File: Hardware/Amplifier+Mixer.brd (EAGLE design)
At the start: 140 x 140 mm, 194 parts, among them IC1 7812, IC2 7805, IC3 7912, IC4 OPA134PA, IC5 OPA134PA, IC6 MEGA8-AI, IC8 LM358D, IC9 LM358D, J1 6MM, J10 JST-XH2, J2 6MM, J3 6MM, J4 6MM, J5 TERMINAL-BLOCK-2PLUG-IN, J6 TERMINAL-BLOCK-2PLUG-IN, J7 ENCODER, J8 DISPLAY, J9 USB, K1 12V 8A, K2 12V 8A, T1 BC817, T2 BC817, T3 BC817, U1 LM1117-3.3, U2 10k, U3 10k, U4 10k, U5 10k, U6 TDA7498L, U7 10k, U8 10k, U9 MCP9700SMD, X1 RCA-4-CHANNEL, X2 JST-XH2, X3 ICSP, X4 JST-XH2

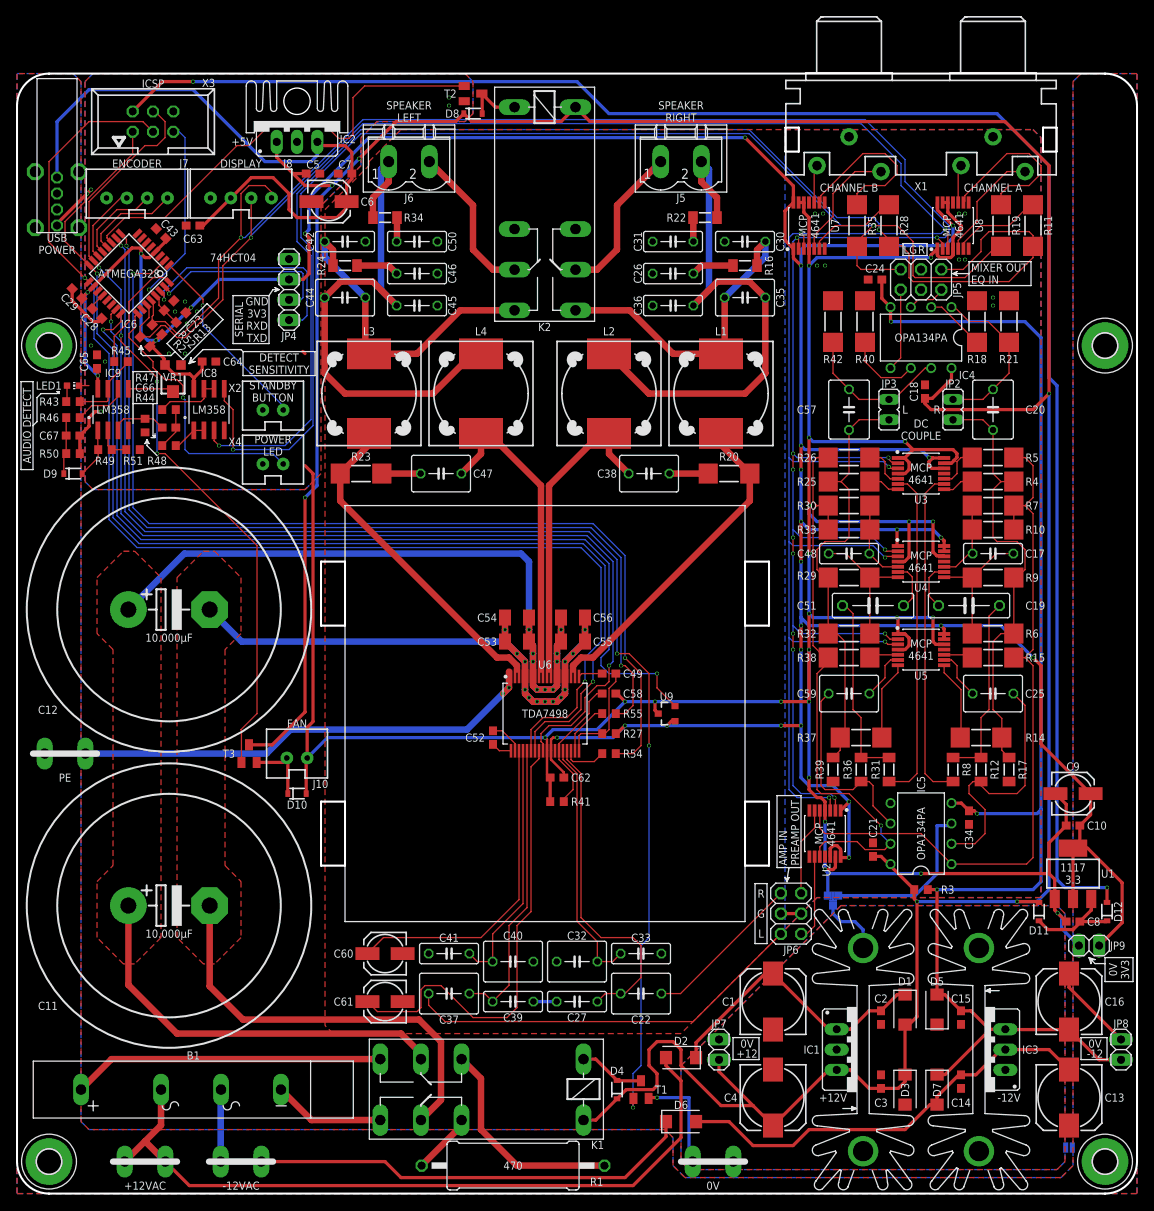
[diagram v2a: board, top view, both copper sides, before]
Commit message: moved power led to pwm capable pin
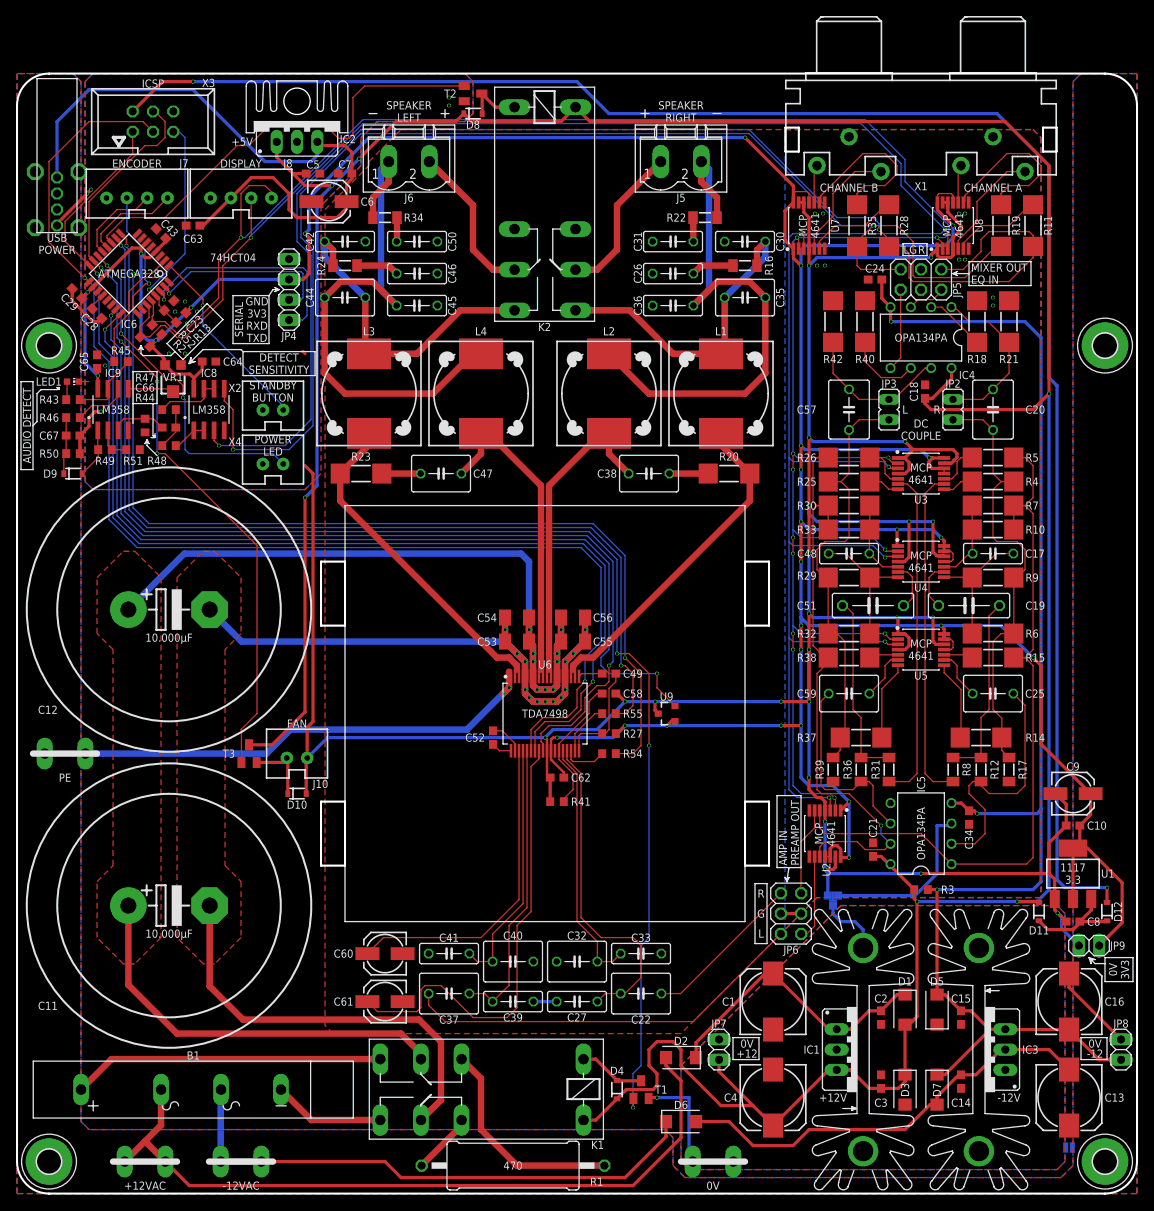
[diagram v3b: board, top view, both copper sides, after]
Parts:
- moved LED1 0.50 mm to (7.00, 101.5)
- moved R43 0.25 mm to (7.00, 99.2)
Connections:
- removed net N$45: IC6.14, J7.2
- new net ENC_BTN: IC6.25, J7.2
- net POWER_LED: now also IC6.14; no longer IC6.25
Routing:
- net ENC_BTN: track 0.00 -> 16.9 mm, vias 0 -> 1
- net +3V3: track 446.6 -> 461.5 mm
- net N$45: track 9.73 -> 0.00 mm
- net POWER_LED: track 34.2 -> 42.4 mm, vias 1 -> 3
- net T_SENSE: track 117.2 -> 116.2 mm
- net AUDIO_DETECT: track 14.8 -> 15.5 mm
- net DGND: vias 35 -> 34

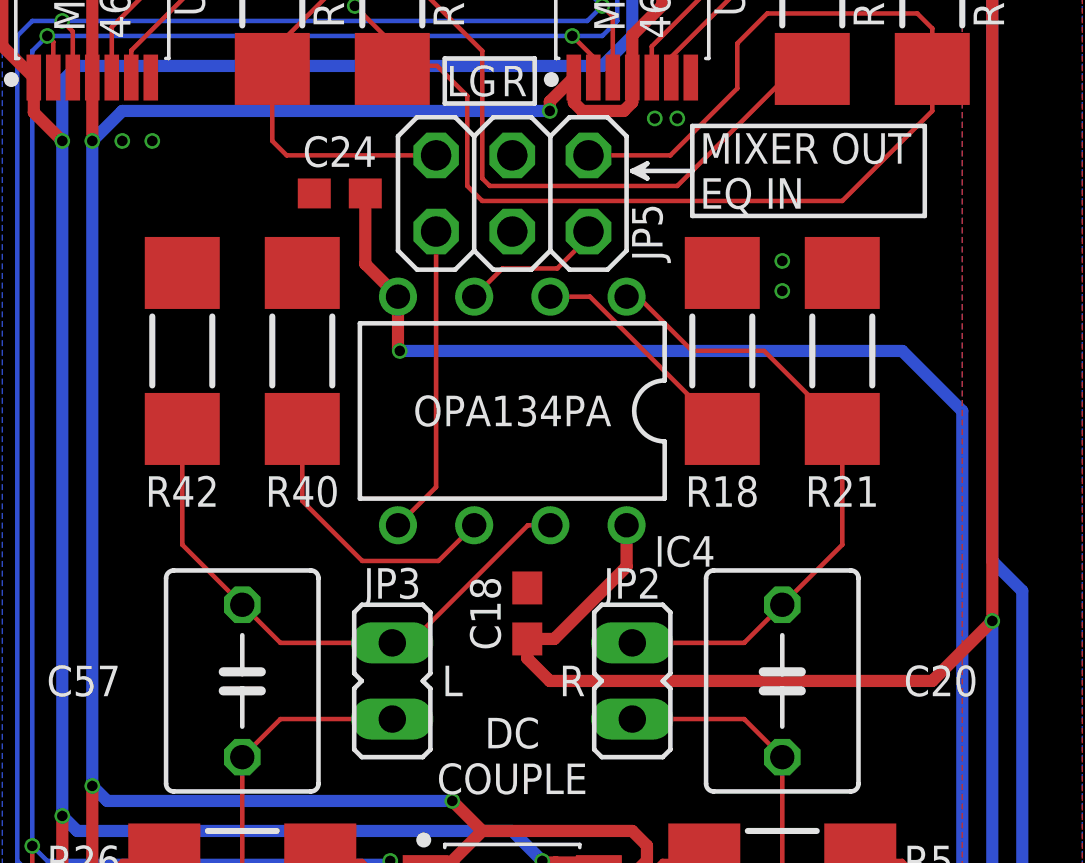
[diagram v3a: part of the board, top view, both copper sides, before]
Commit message: fixed feedback network in mixer buffer output stage
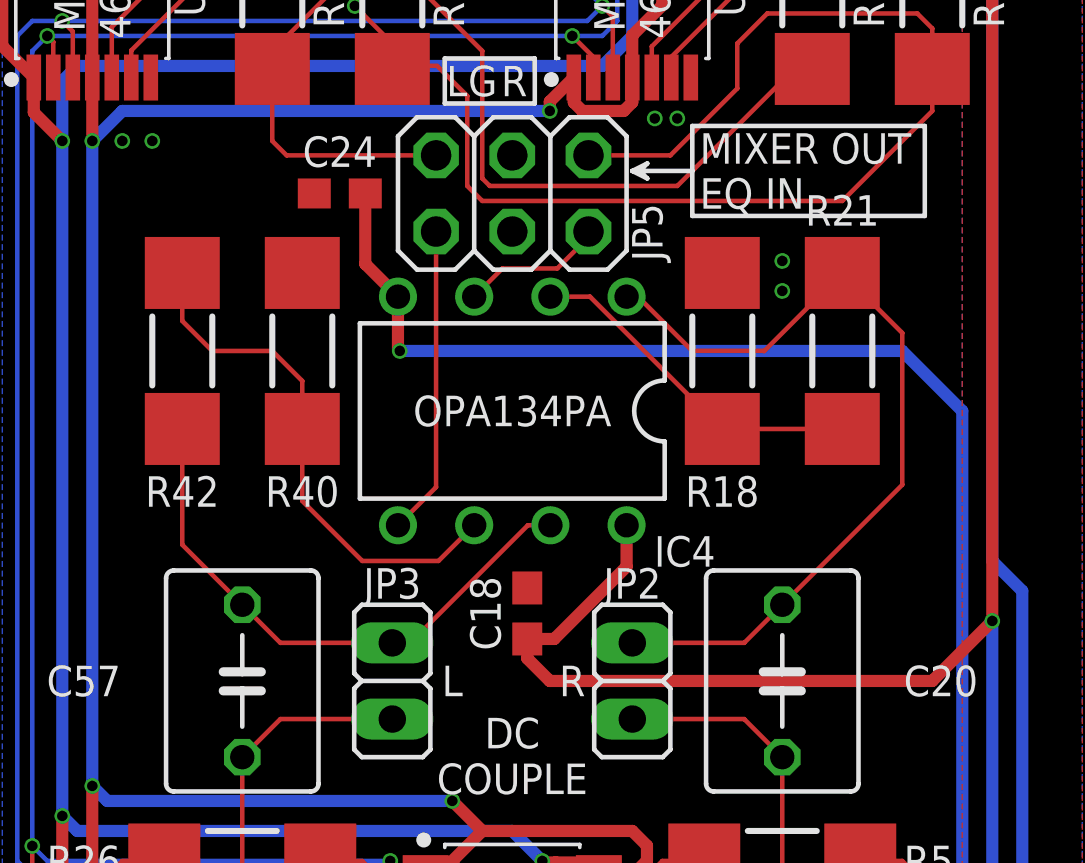
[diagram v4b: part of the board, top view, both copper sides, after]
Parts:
- added U$1: (no value), AdapterBoard:LOGO-SILKSCREEN
- IC4, IC5: value OPA134PA -> LME49720NA
- U9: value MCP9700SMD -> MCP9701SMD
- turned R21 to 270 degrees
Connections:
- removed net N$52: IC4.2, R18.1
- new net N$45: IC4.2, R18.1, R21.2
- net AGND: no longer R21.2, R42.2
- net N$44: now also R42.2
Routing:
- net N$45: track 0.00 -> 11.6 mm
- net N$44: track 9.45 -> 17.5 mm
- net N$52: track 7.56 -> 0.00 mm
- net MIX_AMP_R: track 21.2 -> 28.1 mm
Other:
- board text added: "+3V3"
- board text added: "AVR ICSP"
- board text added: "Amp In"
- board text added: "BTN"
- board text added: "Class D Amplifier 100W + 100 W"
- board text added: "Couple"
- board text added: "DC"
- board text added: "DC+"
- board text added: "DC-"
- board text added: "E A"
- board text added: "E B"
- board text added: "EQ In"
- board text added: "GND"
- board text added: "Mixer Out"
- board text added: "Preamp Out"
- board text added: "RXD"
- board text added: "SCL"
- board text added: "SDA"
- board text added: "Speaker Left"
- board text added: "Speaker Right"
- board text added: "TXD"
- board text added: "V+"
- board text added: "V-"
- board text added: "nupo-artworks.de"
- board text added: "~V+"
- board text added: "~V-"

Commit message: updated to newest version
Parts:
- IC1: value 7812 -> LM2940CT-12
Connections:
- new net VDD: C62.2, R27.2, U6.26
- net +3V3: no longer C62.2, R27.2, U6.26
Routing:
- net +3V3: track 461.5 -> 437.3 mm, vias 27 -> 25
- net VDD: track 0.00 -> 16.1 mm, vias 0 -> 2
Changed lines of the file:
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@@
 <setting verticaltext="up"/>
 </settings>
-<grid distance="1" unitdist="mm" unit="mm" style="lines" multiple="1" display="yes" altdistance="0.25" altunitdist="mm" altunit="mm"/>
+<grid distance="1" unitdist="mm" unit="mm" style="lines" multiple="1" display="yes" altdistance="0.5" altunitdist="mm" altunit="mm"/>
 <layers>
 <layer number="1" name="Top" color="4" fill="1" visible="yes" active="yes"/>
@@
 <attribute name="STOCK" value="4" x="4" y="4" size="1.778" layer="27" display="off"/>
 </element>
-<element name="IC1" library="v-reg" library_urn="urn:adsk.eagle:library:409" package="78XXS" package3d_urn="urn:adsk.eagle:package:30342/1" value="7812" x="105" y="18" smashed="yes" rot="R270">
-<attribute name="CONRAD" value="179230 - 62" x="105" y="18" size="1.778" layer="27" rot="R270" display="off"/>
+<element name="IC1" library="v-reg" library_urn="urn:adsk.eagle:library:409" package="78XXS" package3d_urn="urn:adsk.eagle:package:30342/1" value="LM2940CT-12" x="105" y="18" smashed="yes" rot="R270">
+<attribute name="CONRAD" value="1013996 - 62" x="105" y="18" size="1.778" layer="27" rot="R270" display="off"/>
 <attribute name="MOUSER" value="511-L7812CV" x="105" y="18" size="1.778" layer="27" rot="R270" display="off"/>
 <attribute name="NAME" x="100.3558" y="18" size="1.016" layer="25" ratio="14" align="center-right"/>
@@
 <contactref element="C9" pad="+"/>
 <contactref element="C10" pad="1"/>
-<contactref element="R27" pad="2"/>
-<contactref element="C62" pad="2"/>
 <contactref element="U7" pad="1"/>
 <contactref element="U8" pad="14"/>
@@
 <contactref element="R2" pad="2"/>
 <contactref element="R52" pad="2"/>
-<contactref element="U6" pad="26"/>
 <wire x1="10.095" y1="100.6" x2="10.095" y2="102.25" width="0.4064" layer="1"/>
 <wire x1="16.601040625" y1="105.89895625" x2="17.35104375" y2="106.648959375" width="0.4064" layer="1"/>
@@
 <wire x1="102.95" y1="42.1134" x2="102.95" y2="43.05" width="0.4064" layer="1"/>
 <wire x1="102.95" y1="43.05" x2="102.5" y2="43.5" width="0.4064" layer="1"/>
-<wire x1="74.85" y1="57.5" x2="75" y2="57.5" width="0.4064" layer="1"/>
-<wire x1="75" y1="57.5" x2="76" y2="58.5" width="0.4064" layer="1"/>
-<via x="76" y="58.5" extent="1-16" drill="0.35" shape="octagon"/>
-<wire x1="95.5" y1="58.5" x2="81.25" y2="58.5" width="0.4064" layer="16"/>
+<wire x1="95.5" y1="58.5" x2="83.25" y2="58.5" width="0.4064" layer="16"/>
 <via x="95.5" y="58.5" extent="1-16" drill="0.35" shape="octagon"/>
-<wire x1="81.25" y1="58.5" x2="76" y2="58.5" width="0.4064" layer="16"/>
 <wire x1="98" y1="58.5" x2="95.5" y2="58.5" width="0.4064" layer="1"/>
 <via x="98" y="58.5" extent="1-16" drill="0.35" shape="octagon"/>
-<wire x1="66.75" y1="55.3545" x2="66.75" y2="56.75" width="0.3048" layer="1"/>
-<wire x1="66.75" y1="56.75" x2="67" y2="57" width="0.3048" layer="1"/>
-<wire x1="67" y1="57" x2="67.5" y2="57" width="0.3048" layer="1"/>
-<via x="67.5" y="57" extent="1-16" drill="0.35" shape="octagon"/>
-<wire x1="67.5" y1="57" x2="74.5" y2="57" width="0.4064" layer="16"/>
-<wire x1="74.5" y1="57" x2="76" y2="58.5" width="0.4064" layer="16"/>
-<wire x1="66.75" y1="55.3545" x2="66.75" y2="54.25" width="0.3048" layer="1"/>
-<wire x1="68.35" y1="52.65" x2="68.35" y2="52" width="0.3048" layer="1"/>
-<wire x1="66.75" y1="54.25" x2="68.35" y2="52.65" width="0.3048" layer="1"/>
 <via x="15.5" y="117.5" extent="1-16" drill="0.35" shape="octagon"/>
 <wire x1="17.31816875" y1="117.75248125" x2="16.5656875" y2="117" width="0.4064" layer="1"/>
@@
 <wire x1="18.374996875" y1="103.700003125" x2="18.5" y2="103.575" width="0.4064" layer="1"/>
 <contactref element="U9" pad="1"/>
-<via x="81.25" y="58.5" extent="1-16" drill="0.35" shape="octagon"/>
-<wire x1="81.25" y1="58.5" x2="81.8" y2="59.05" width="0.4064" layer="1"/>
-<wire x1="81.8" y1="59.05" x2="82.25" y2="59.05" width="0.4064" layer="1"/>
+<via x="83.25" y="58.5" extent="1-16" drill="0.35" shape="octagon"/>
+<wire x1="83.25" y1="58.5" x2="82.7" y2="59.05" width="0.4064" layer="1"/>
+<wire x1="82.25" y1="59.05" x2="82.7" y2="59.05" width="0.4064" layer="1"/>
 <contactref element="U4" pad="11"/>
 <contactref element="U5" pad="11"/>
@@
 <wire x1="120" y1="106.4" x2="124" y2="106.4" width="0.1524" layer="1"/>
 </signal>
+<signal name="VDD">
+<contactref element="R27" pad="2"/>
+<contactref element="U6" pad="26"/>
+<contactref element="C62" pad="2"/>
+<wire x1="68.35" y1="52.65" x2="68.35" y2="52" width="0.3048" layer="1"/>
+<wire x1="67" y1="54" x2="68.35" y2="52.65" width="0.3048" layer="1"/>
+<wire x1="74.85" y1="57.5" x2="75.5" y2="57.5" width="0.4064" layer="1"/>
+<wire x1="75.5" y1="57.5" x2="76" y2="57" width="0.4064" layer="1"/>
+<via x="76" y="57" extent="1-16" drill="0.35" shape="octagon"/>
+<wire x1="76" y1="57" x2="67" y2="57" width="0.4064" layer="16"/>
+<via x="67" y="57" extent="1-16" drill="0.35" shape="octagon"/>
+<wire x1="66.75" y1="55.3545" x2="66.75" y2="56.75" width="0.3048" layer="1"/>
+<wire x1="66.75" y1="56.75" x2="67" y2="57" width="0.3048" layer="1"/>
+<wire x1="66.75" y1="55.3545" x2="66.75" y2="54.25" width="0.3048" layer="1"/>
+<wire x1="66.75" y1="54.25" x2="67" y2="54" width="0.3048" layer="1"/>
+</signal>
 </signals>
